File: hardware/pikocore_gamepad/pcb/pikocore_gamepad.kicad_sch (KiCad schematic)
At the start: 0 parts

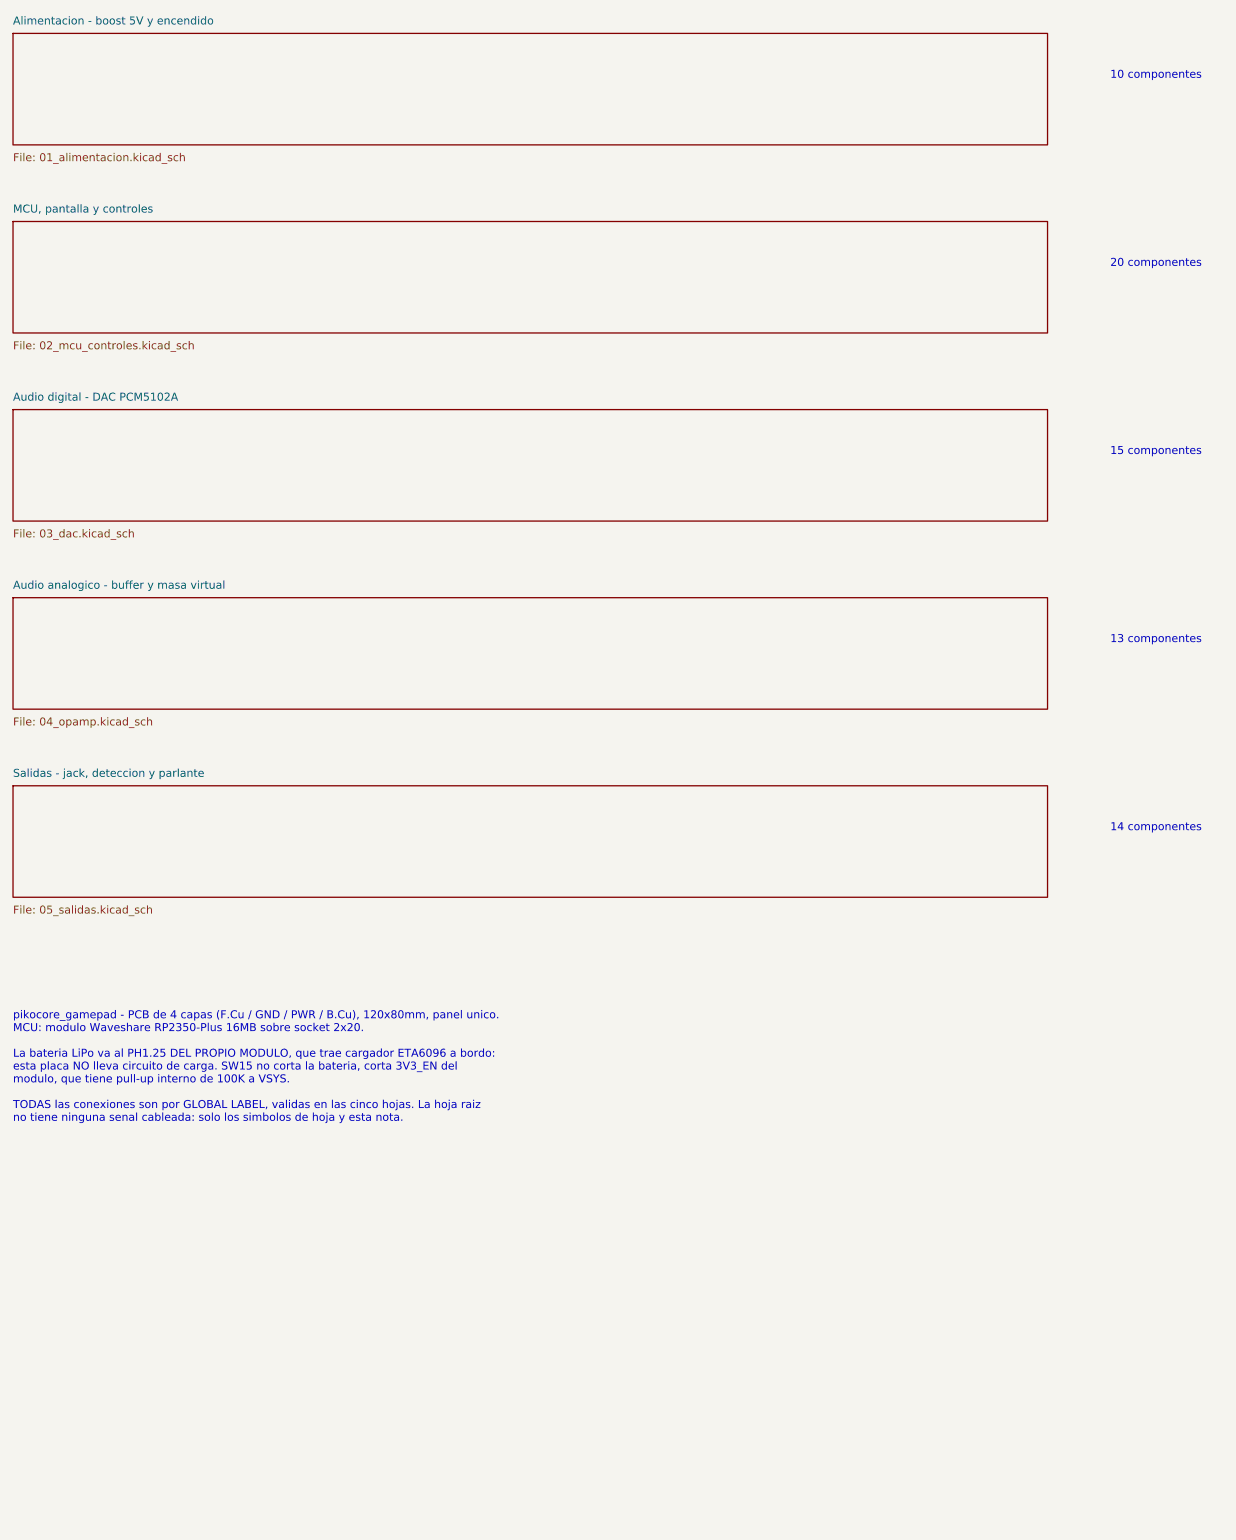
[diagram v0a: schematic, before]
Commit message: hw: RP2350A chip-down en la placa (reemplaza el modulo RP2350-Plus)
El modulo Waveshare RP2350-Plus sale y su circuito pasa al dorso:
RP2350A QFN-60 con el nucleo de la placa minima oficial de Raspberry Pi
(MIT) copiado como bloque rigido (import_rp_minimal.py -> rp_core_ref.py,
colocado por rp_core.py), flash W25Q128, cristal 12 MHz, USB-C, cargador
ETA6096, OR de alimentacion con MBR230, buck-boost TPS63001 a 3V3,
botones BOOTSEL/RUN y pads SWD. GP0-22/GP26 sin cambios; GP23/24/29
nuevos (BB_PS, VBUS_SENSE, VSYS_ADC) tambien en config.h.

Ruteo:
- El cobre previo (nucleo, pistas manuales, vias a plano) va al DSN
  protegido; las zonas del nucleo en la cara del chip van como keepout.
- Segunda pasada de freerouting solo si deja menos conexiones abiertas.
- Senales a 0.127/0.127 con via 0.45/0.2; Power con via propia 0.6/0.3.
- Carriles de salida de la placa oficial para LCD_DC, LCD_MOSI,
  BTN_START y DPAD_UP/DOWN; pin 1 de U1 al anillo de 3V3 a mano.
- TPS63001 a 180 grados con L1/L2 a mano; GND y VBUS del USB-C a mano.

Puertas: 191 tests, ERC 0, DRC 0 errores / 0 sin conectar / 0 paridad
(9 avisos previos), G-5/G-4/G-2/placement en verde. G-0 sigue en rojo
solo por LCD_FPC_PIN_ORDER, como en main. Sin verificar: LCSC de R31
(ISET 150k), saturacion de L4, rotaciones del CPL de las piezas nuevas.

Co-Authored-By: Claude Opus 5.5 <noreply@anthropic.com>
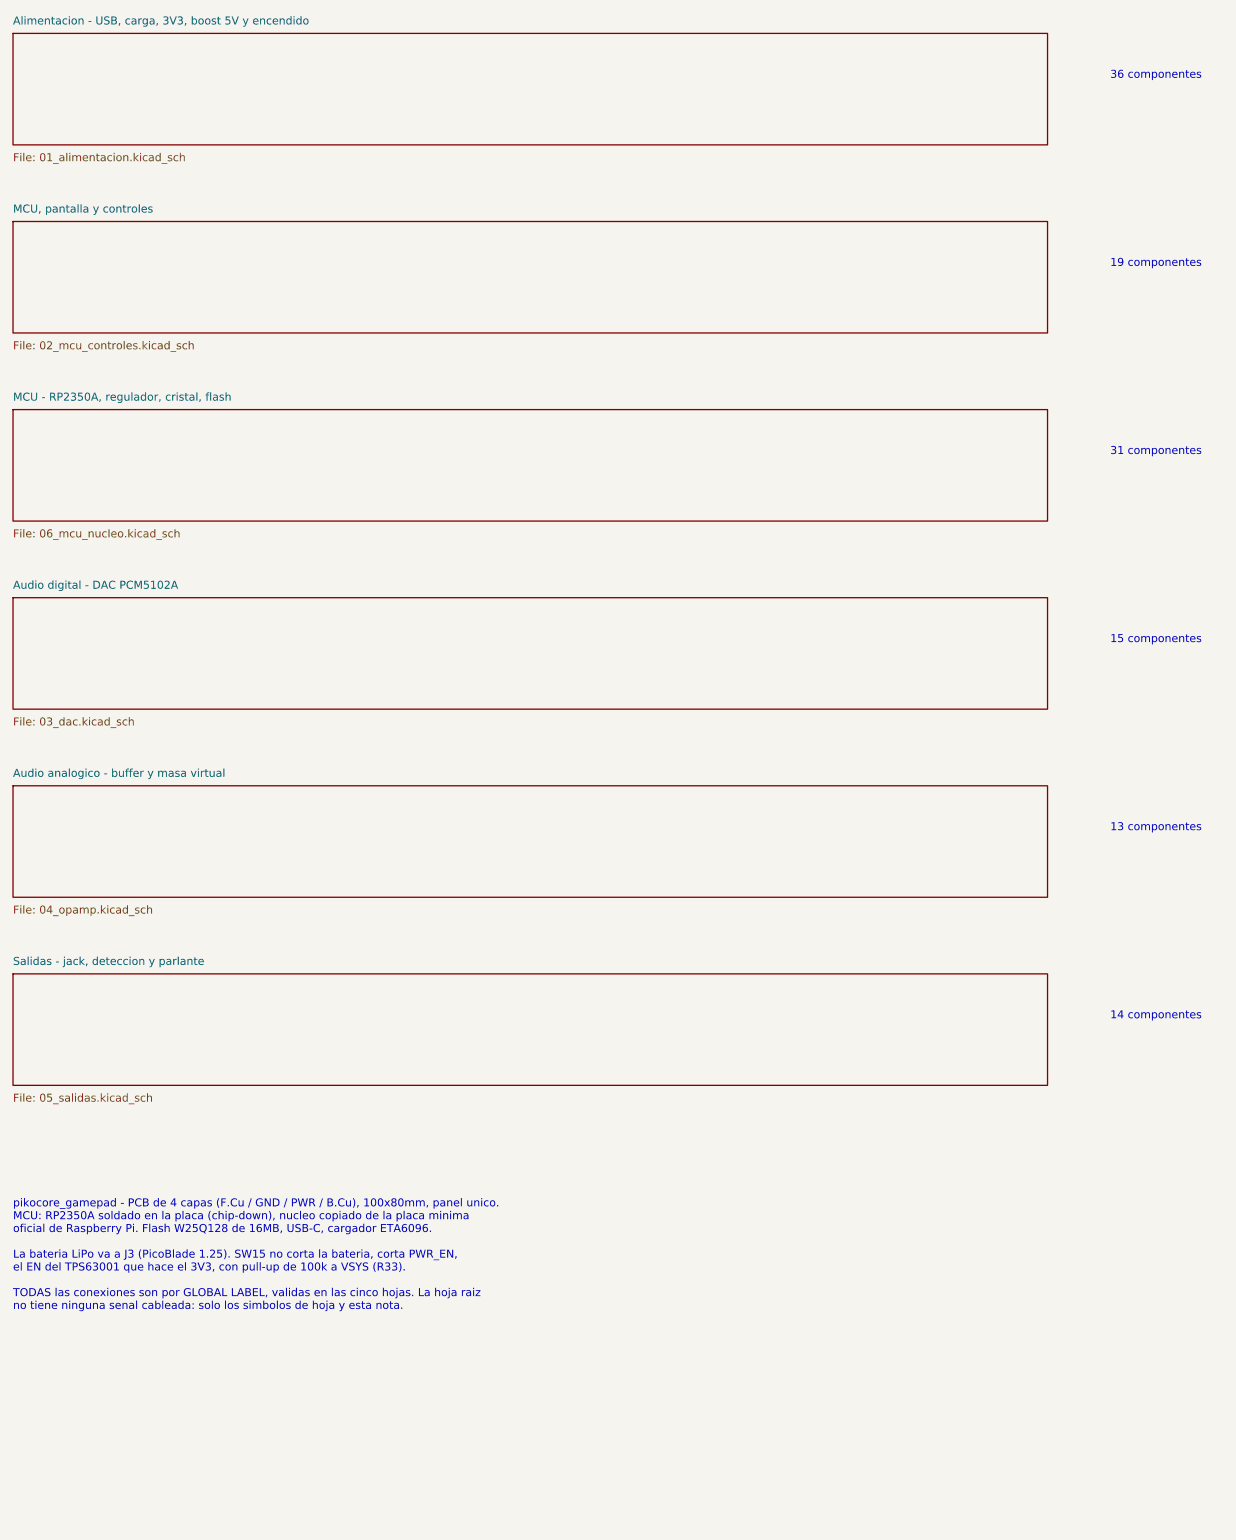
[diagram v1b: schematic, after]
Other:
- sheet Alimentacion - boost 5V y encendido renamed Alimentacion - USB, carga, 3V3, boost 5V y encendido
- added sheet MCU - RP2350A, regulador, cristal, flash (06_mcu_nucleo.kicad_sch)
- note added: "19 componentes"
- note added: "31 componentes"
- note added: "36 componentes"
- note added: "pikocore_gamepad - PCB de 4 capas (F.Cu / GND / PWR / B.Cu), 100x80mm, panel unico. MCU: RP2350A soldado en la placa (chip-down), nucleo copiado de la placa minima oficial de Raspberry Pi. Flash W25Q128 de 16MB, USB-C, cargador ETA6096. La bateria LiPo va a J3 (PicoBlade 1.25). SW15 no corta la bateria, corta PWR_EN, el EN del TPS63001 que hace el 3V3, con pull-up de 100k a VSYS (R33). TODAS las 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"
- note removed: "10 componentes"
- note removed: "20 componentes"
- note removed: "pikocore_gamepad - PCB de 4 capas (F.Cu / GND / PWR / B.Cu), 120x80mm, panel unico. MCU: modulo Waveshare RP2350-Plus 16MB sobre socket 2x20. La bateria LiPo va al PH1.25 DEL PROPIO MODULO, que trae cargador ETA6096 a bordo: esta placa NO lleva circuito de carga. SW15 no corta la bateria, corta 3V3_EN del modulo, que tiene pull-up interno de 100K a VSYS. TODAS las conexiones son por GLOBAL LABEL,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"
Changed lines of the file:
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@@
     (date "2026-08-28")
     (rev "A")
-    (comment 1 "MCU: Waveshare RP2350-Plus 16MB en socket | LiPo al PH1.25 del modulo")
+    (comment 1 "MCU: RP2350A chip-down (nucleo de la placa minima oficial) | LiPo en J3")
     (comment 2 "Pinout: pinmap.py, verificado contra el firmware por la puerta G-4")
   )
@@
     (stroke (width 0.1524) (type solid))
     (fill (color 0 0 0 0.0))
-    (property "Sheetname" "Alimentacion - boost 5V y encendido" (at 30 23.73 0)
+    (property "Sheetname" "Alimentacion - USB, carga, 3V3, boost 5V y encendido" (at 30 23.73 0)
       (effects (font (size 1.27 1.27)) (justify left bottom))
     )
@@
     )
   )
-  (text "10 componentes" (exclude_from_sim no) (at 205 31 0)
+  (text "36 componentes" (exclude_from_sim no) (at 205 31 0)
     (effects (font (size 1.27 1.27)) (justify left top))
   )
@@
     )
   )
-  (text "20 componentes" (exclude_from_sim no) (at 205 61 0)
+  (text "19 componentes" (exclude_from_sim no) (at 205 61 0)
     (effects (font (size 1.27 1.27)) (justify left top))
   )
@@
     (stroke (width 0.1524) (type solid))
     (fill (color 0 0 0 0.0))
-    (property "Sheetname" "Audio digital - DAC PCM5102A" (at 30 83.73 0)
+    (property "Sheetname" "MCU - RP2350A, regulador, cristal, flash" (at 30 83.73 0)
       (effects (font (size 1.27 1.27)) (justify left bottom))
     )
-    (property "Sheetfile" "03_dac.kicad_sch" (at 30 104.05 0)
+    (property "Sheetfile" "06_mcu_nucleo.kicad_sch" (at 30 104.05 0)
       (effects (font (size 1.27 1.27)) (justify left top))
     )
@@
     )
   )
-  (text "15 componentes" (exclude_from_sim no) (at 205 91 0)
+  (text "31 componentes" (exclude_from_sim no) (at 205 91 0)
     (effects (font (size 1.27 1.27)) (justify left top))
   )
@@
     (stroke (width 0.1524) (type solid))
     (fill (color 0 0 0 0.0))
-    (property "Sheetname" "Audio analogico - buffer y masa virtual" (at 30 113.73 0)
+    (property "Sheetname" "Audio digital - DAC PCM5102A" (at 30 113.73 0)
       (effects (font (size 1.27 1.27)) (justify left bottom))
     )
-    (property "Sheetfile" "04_opamp.kicad_sch" (at 30 134.05 0)
+    (property "Sheetfile" "03_dac.kicad_sch" (at 30 134.05 0)
       (effects (font (size 1.27 1.27)) (justify left top))
     )
@@
     )
   )
-  (text "13 componentes" (exclude_from_sim no) (at 205 121 0)
+  (text "15 componentes" (exclude_from_sim no) (at 205 121 0)
     (effects (font (size 1.27 1.27)) (justify left top))
   )
@@
     (stroke (width 0.1524) (type solid))
     (fill (color 0 0 0 0.0))
-    (property "Sheetname" "Salidas - jack, deteccion y parlante" (at 30 143.73 0)
+    (property "Sheetname" "Audio analogico - buffer y masa virtual" (at 30 143.73 0)
       (effects (font (size 1.27 1.27)) (justify left bottom))
     )
-    (property "Sheetfile" "05_salidas.kicad_sch" (at 30 164.05 0)
+    (property "Sheetfile" "04_opamp.kicad_sch" (at 30 164.05 0)
       (effects (font (size 1.27 1.27)) (justify left top))
     )
@@
     )
   )
-  (text "14 componentes" (exclude_from_sim no) (at 205 151 0)
+  (text "13 componentes" (exclude_from_sim no) (at 205 151 0)
     (effects (font (size 1.27 1.27)) (justify left top))
   )
-  (text "pikocore_gamepad - PCB de 4 capas (F.Cu / GND / PWR / B.Cu), 120x80mm, panel unico.\nMCU: modulo Waveshare RP2350-Plus 16MB sobre socket 2x20.\n\nLa bateria LiPo va al PH1.25 DEL PROPIO MODULO, que trae cargador ETA6096 a bordo:\nesta placa NO lleva circuito de carga. SW15 no corta la bateria, corta 3V3_EN del\nmodulo, que tiene pull-up interno de 100K a VSYS.\n\nTODAS las conexiones son por GLOBAL LABEL, validas en las cinco hojas. La hoja raiz\nno tiene ninguna senal cableada: solo los simbolos de hoja y esta nota." (exclude_from_sim no) (at 30 181 0)
+  (sheet (at 30 175) (size 165 17.78)
+    (stroke (width 0.1524) (type solid))
+    (fill (color 0 0 0 0.0))
+    (property "Sheetname" "Salidas - jack, deteccion y parlante" (at 30 173.73 0)
+      (effects (font (size 1.27 1.27)) (justify left bottom))
+    )
+    (property "Sheetfile" "05_salidas.kicad_sch" (at 30 194.05 0)
+      (effects (font (size 1.27 1.27)) (justify left top))
+    )
+    (instances
+      (project "pikocore_gamepad"
+        (path "/b1e7c2a4-9f31-4d6e-8a52-3c0f7d418e6b" (page "7"))
+      )
+    )
+  )
+  (text "14 componentes" (exclude_from_sim no) (at 205 181 0)
     (effects (font (size 1.27 1.27)) (justify left top))
   )
+  (text "pikocore_gamepad - PCB de 4 capas (F.Cu / GND / PWR / B.Cu), 100x80mm, panel unico.\nMCU: RP2350A soldado en la placa (chip-down), nucleo copiado de la placa minima\noficial de Raspberry Pi. Flash W25Q128 de 16MB, USB-C, cargador ETA6096.\n\nLa bateria LiPo va a J3 (PicoBlade 1.25). SW15 no corta la bateria, corta PWR_EN,\nel EN del TPS63001 que hace el 3V3, con pull-up de 100k a VSYS (R33).\n\nTODAS las conexiones son por GLOBAL LABEL, validas en las cinco hojas. La hoja raiz\nno tiene ninguna senal cableada: solo los simbolos de hoja y esta nota." (exclude_from_sim no) (at 30 211 0)
+    (effects (font (size 1.27 1.27)) (justify left top))
+  )

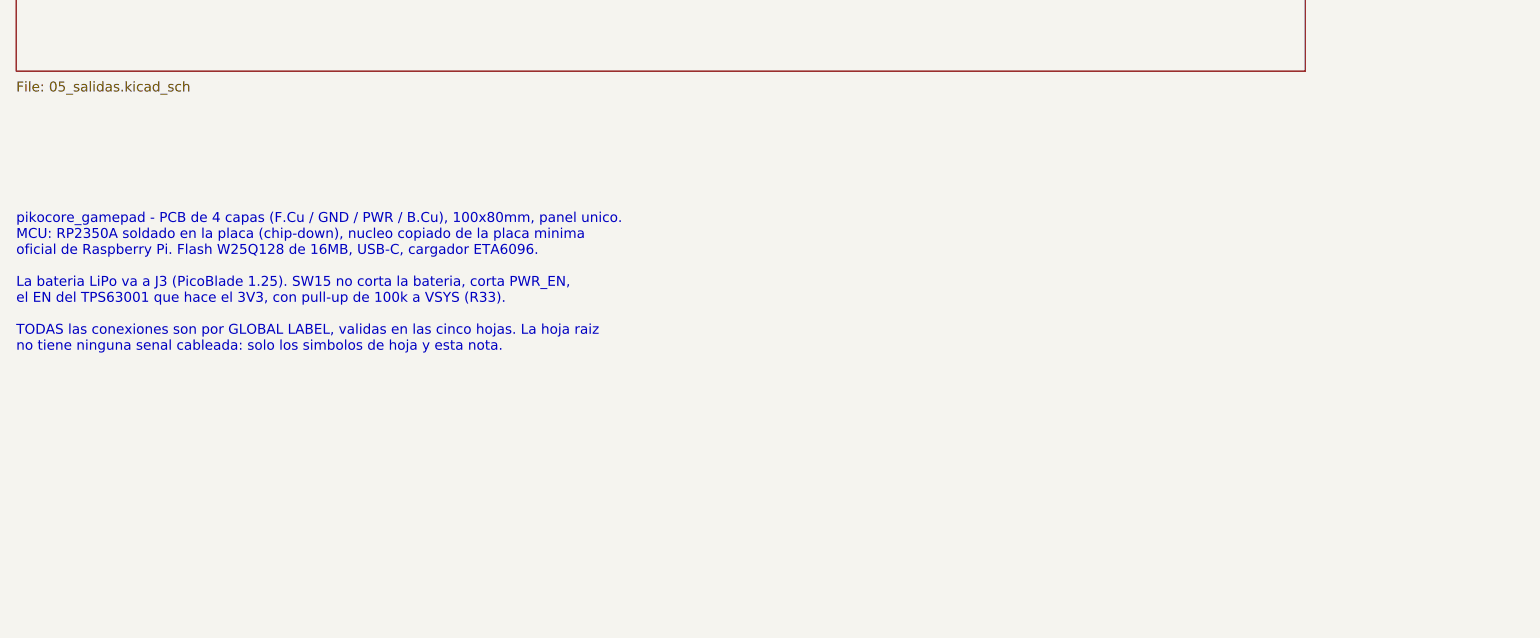
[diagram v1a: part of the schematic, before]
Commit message: hw: hoja 07_midi en el esquematico
Co-Authored-By: Claude Fable 5.1 <noreply@anthropic.com>
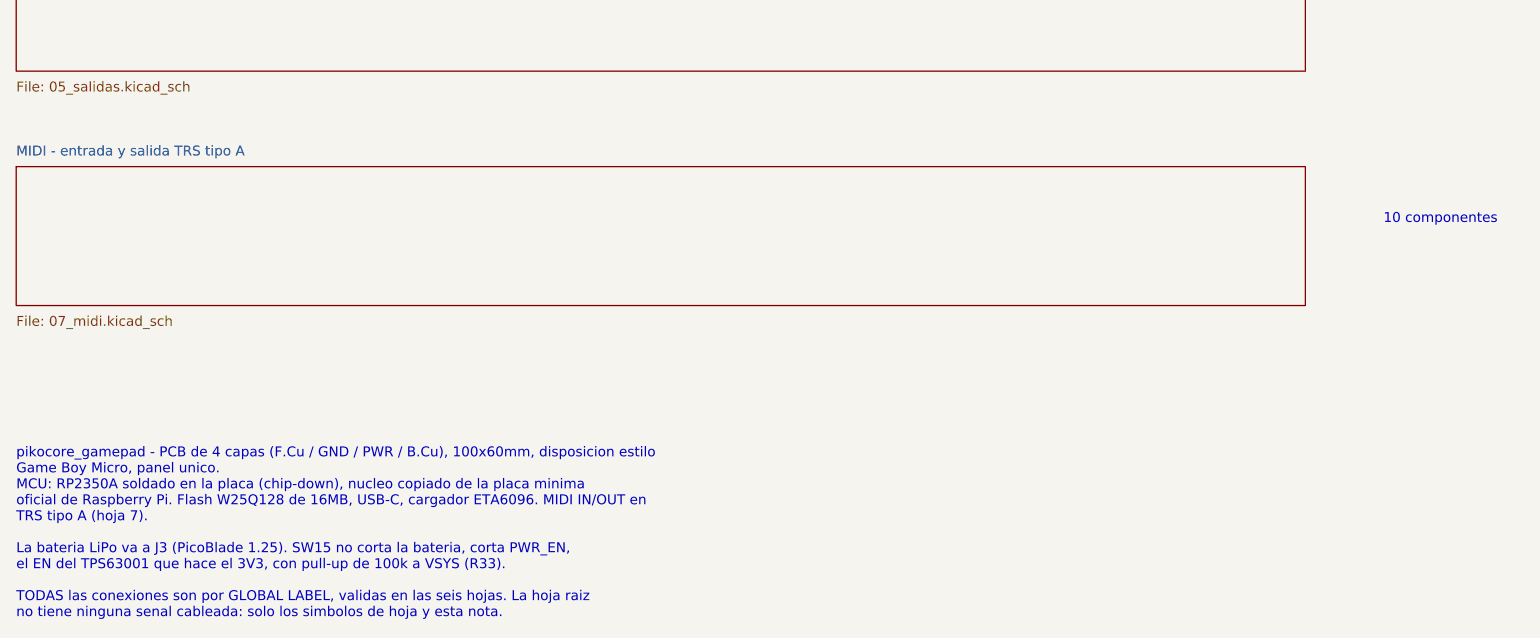
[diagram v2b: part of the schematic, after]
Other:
- added sheet MIDI - entrada y salida TRS tipo A (07_midi.kicad_sch)
- note added: "10 componentes"
- note added: "pikocore_gamepad - PCB de 4 capas (F.Cu / GND / PWR / B.Cu), 100x60mm, disposicion estilo Game Boy Micro, panel unico. MCU: RP2350A soldado en la placa (chip-down), nucleo copiado de la placa minima oficial de Raspberry Pi. Flash W25Q128 de 16MB, USB-C, cargador ETA6096. MIDI IN/OUT en TRS tipo A (hoja 7). La bateria LiPo va a J3 (PicoBlade 1.25). SW15 no corta la bateria, corta PWR_EN, el EN del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"
- note removed: "pikocore_gamepad - PCB de 4 capas (F.Cu / GND / PWR / B.Cu), 100x80mm, panel unico. MCU: RP2350A soldado en la placa (chip-down), nucleo copiado de la placa minima oficial de Raspberry Pi. Flash W25Q128 de 16MB, USB-C, cargador ETA6096. La bateria LiPo va a J3 (PicoBlade 1.25). SW15 no corta la bateria, corta PWR_EN, el EN del TPS63001 que hace el 3V3, con pull-up de 100k a VSYS (R33). TODAS las 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"
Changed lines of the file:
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@@
     (effects (font (size 1.27 1.27)) (justify left top))
   )
-  (text "pikocore_gamepad - PCB de 4 capas (F.Cu / GND / PWR / B.Cu), 100x80mm, panel unico.\nMCU: RP2350A soldado en la placa (chip-down), nucleo copiado de la placa minima\noficial de Raspberry Pi. Flash W25Q128 de 16MB, USB-C, cargador ETA6096.\n\nLa bateria LiPo va a J3 (PicoBlade 1.25). SW15 no corta la bateria, corta PWR_EN,\nel EN del TPS63001 que hace el 3V3, con pull-up de 100k a VSYS (R33).\n\nTODAS las conexiones son por GLOBAL LABEL, validas en las cinco hojas. La hoja raiz\nno tiene ninguna senal cableada: solo los simbolos de hoja y esta nota." (exclude_from_sim no) (at 30 211 0)
+  (sheet (at 30 205) (size 165 17.78)
+    (stroke (width 0.1524) (type solid))
+    (fill (color 0 0 0 0.0))
+    (property "Sheetname" "MIDI - entrada y salida TRS tipo A" (at 30 203.73 0)
+      (effects (font (size 1.27 1.27)) (justify left bottom))
+    )
+    (property "Sheetfile" "07_midi.kicad_sch" (at 30 224.05 0)
+      (effects (font (size 1.27 1.27)) (justify left top))
+    )
+    (instances
+      (project "pikocore_gamepad"
+        (path "/b1e7c2a4-9f31-4d6e-8a52-3c0f7d418e6b" (page "8"))
+      )
+    )
+  )
+  (text "10 componentes" (exclude_from_sim no) (at 205 211 0)
     (effects (font (size 1.27 1.27)) (justify left top))
   )
+  (text "pikocore_gamepad - PCB de 4 capas (F.Cu / GND / PWR / B.Cu), 100x60mm, disposicion estilo\nGame Boy Micro, panel unico.\nMCU: RP2350A soldado en la placa (chip-down), nucleo copiado de la placa minima\noficial de Raspberry Pi. Flash W25Q128 de 16MB, USB-C, cargador ETA6096. MIDI IN/OUT en\nTRS tipo A (hoja 7).\n\nLa bateria LiPo va a J3 (PicoBlade 1.25). SW15 no corta la bateria, corta PWR_EN,\nel EN del TPS63001 que hace el 3V3, con pull-up de 100k a VSYS (R33).\n\nTODAS las conexiones son por GLOBAL LABEL, validas en las seis hojas. La hoja raiz\nno tiene ninguna senal cableada: solo los simbolos de hoja y esta nota." (exclude_from_sim no) (at 30 241 0)
+    (effects (font (size 1.27 1.27)) (justify left top))
+  )
